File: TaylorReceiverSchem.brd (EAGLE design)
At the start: 51.7 x 73.7 mm, 16 parts, among them U1 TEENSY_3.1_BASIC, U2 XBEE_ADAPTER_KIT

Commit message: Improved PCB Routing
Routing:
- net STRIP7: track 90.1 -> 71.8 mm, vias 1 -> 0
- net 3.3V: track 41.7 -> 53.2 mm, vias 1 -> 0
- net VCC: track 41.1 -> 30.4 mm, vias 2 -> 0
- net STRIP2: track 57.8 -> 49.1 mm
- net STRIP1: track 38.5 -> 47.1 mm, vias 1 -> 0
- net GND: track 8.19 -> 0.00 mm
- net STRIP3: track 36.0 -> 43.4 mm, vias 1 -> 0
- net N$4: track 57.2 -> 52.3 mm, vias 1 -> 0
- net STRIP6: track 50.6 -> 46.6 mm, vias 0 -> 1
- net N$9: track 24.7 -> 26.2 mm
- net N$7: track 10.8 -> 12.3 mm
- net N$6: track 13.3 -> 14.8 mm
- net N$10: track 22.2 -> 23.7 mm
- net STRIP8: track 56.7 -> 55.5 mm
- net N$1: track 3.07 -> 2.54 mm

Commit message: New and improved board design
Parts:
- removed R4, R5, R6, R7, R8: (no value), SparkFun-Resistors:AXIAL-0.4
- added C3, C4: (no value), SparkFun-Capacitors:CAP-PTH-5MM
- added D1, D2, D3: (no value), SparkFun-LED:LED5MM
- added F1: (no value), fuse:SHK20L
- added RN1: (no value), resistor-dil:DIL16
- added SW1: (no value), special:EDG-04
- added U3: XBEE-1B1, SparkFun-RF:XBEE-1
- R1, R2, R3: device SparkFun-Resistors:AXIAL-0.4 -> SparkFun-Passives:AXIAL-0.3
- U2: value XBEE_ADAPTER_KIT -> V_REG_LDOSMD; device Nanotronics:1X10 -> SparkFun-PowerIC:SOT23-5
- moved C1 41.2 mm to (44.5, 68.6)
- moved U2 35.6 mm to (39.4, 68.6), turned to 180 degrees
- moved C2 18.8 mm to (24.1, 5.08), turned to 90 degrees
- moved JP1 11.4 mm to (58.4, 47.0)
- moved JP2 11.4 mm to (58.4, 20.3)
- moved JP3 11.4 mm to (58.4, 71.1)
- moved R1 6.35 mm to (30.5, 49.5), turned to 90 degrees
- moved R3 5.08 mm to (34.3, 49.5), turned to 90 degrees
- moved R2 3.81 mm to (38.1, 49.5), turned to 90 degrees
- moved JP4 1.27 mm to (33.0, 0.00)
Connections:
- removed net N$4: U1.0, U2.8
- removed net N$5: U1.1, U2.7
- new net ASC: R3.P$1, U3.15
- new net DIP1: SW1.1, U1.9
- new net DIP2: SW1.2, U1.10
- new net DIP3: SW1.3, U1.11
- new net DIP4: SW1.4, U1.12
- new net N$15: D1.A, R1.P$2
- new net N$16: D2.A, R2.P$2
- new net N$17: D3.A, R3.P$2
- new net N$2: F1.1A, JP4.PWR
- new net N$3: C3.1, C4.1, U2.5, U3.1
- new net RSSI: R2.P$1, U3.6
- new net XBEERECV: U1.0, U3.2
- net GND: now also C3.2, C4.2, D1.K, D2.K, D3.K, SW1.5, SW1.6, SW1.7, SW1.8, U3.10, U3.3; no longer U2.4
- net N$10: now also RN1.5; no longer R5.P$1
- net N$11: now also RN1.6; no longer R6.P$1
- net N$12: now also RN1.7; no longer R7.P$1
- net N$13: now also RN1.8; no longer R8.P$1
- net N$6: now also RN1.1; no longer R1.P$1
- net N$7: now also RN1.2; no longer R2.P$1
- net N$8: now also RN1.3; no longer R3.P$1
- net N$9: now also RN1.4; no longer R4.P$1
- net STRIP1: now also RN1.16; no longer R1.P$2
- net STRIP2: now also RN1.15; no longer R2.P$2
- net STRIP3: now also RN1.14; no longer R3.P$2
- net STRIP4: now also RN1.13; no longer R4.P$2
- net STRIP5: now also RN1.12; no longer R5.P$2
- net STRIP6: now also RN1.11; no longer R6.P$2
- net STRIP7: now also RN1.10; no longer R7.P$2
- net STRIP8: now also RN1.9; no longer R8.P$2
- net VCC: now also F1.2A, R1.P$1, U2.3; no longer JP4.PWR, U2.10
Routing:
- net XBEERECV: track 0.00 -> 75.6 mm
- net N$4: track 52.3 -> 0.00 mm
- net N$5: track 52.3 -> 0.00 mm
- net DIP1: track 0.00 -> 50.9 mm, vias 0 -> 1
- net RSSI: track 0.00 -> 43.3 mm
- net N$3: track 0.00 -> 41.0 mm
- net DIP2: track 0.00 -> 36.7 mm
- net DIP3: track 0.00 -> 33.1 mm, vias 0 -> 1
- net VCC: track 30.4 -> 0.00 mm
- net DIP4: track 0.00 -> 28.0 mm
- net N$13: track 8.15 -> 35.4 mm
- net N$12: track 8.15 -> 30.0 mm
- net N$8: track 10.8 -> 31.6 mm
- net STRIP1: track 47.1 -> 27.3 mm
- net STRIP3: track 43.4 -> 24.1 mm
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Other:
- board size 51.7 x 73.7 mm -> 61.9 x 73.7 mm
- board text added: "ASC"
- board text added: "Asher Levine"
- board text added: "David Sheinkopf"
- board text added: "GND"
- board text added: "Power"
- board text added: "RSSI"
- board text added: "VCC"
- board text added: "XBEE"
- board text removed: "Dave Sheinkopf"

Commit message: Added right angle connectors to board.
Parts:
- removed JP1, JP2, JP3: (no value), SparkFun-Connectors:1X08_ROUND
- added P1, P2, P3: 39-30-08?_S, con-molex-mini-fit:39-30-?08?
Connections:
- removed net N$10: JP2.3, RN1.5
- removed net N$11: JP2.1, RN1.6
- new net N$4: P2.5, RN1.5
- new net N$5: P2.2, RN1.6
- net GND: now also P1.3, P1.7, P2.3, P2.7, P3.3, P3.7; no longer JP1.4, JP1.7, JP2.4, JP2.7, JP3.4, JP3.7
- net N$12: now also P3.6; no longer JP3.6
- net N$13: now also P3.5; no longer JP3.3
- net N$6: now also P1.6; no longer JP1.6
- net N$7: now also P1.5; no longer JP1.3
- net N$8: now also P1.2; no longer JP1.1
- net N$9: now also P2.6; no longer JP2.6
- net VCC: now also P1.1, P1.4, P1.8, P2.1, P2.4, P2.8, P3.4, P3.8; no longer JP1.2, JP1.5, JP1.8, JP2.2, JP2.5, JP2.8, JP3.5, JP3.8
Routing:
- net N$6: track 21.2 -> 108.4 mm
- net N$7: track 25.5 -> 89.5 mm
- net N$5: track 0.00 -> 37.5 mm
- net VCC: track 0.00 -> 25.1 mm, vias 0 -> 1
- net N$4: track 0.00 -> 19.4 mm
- net N$10: track 16.6 -> 0.00 mm
- net N$13: track 35.4 -> 19.6 mm
- net N$8: track 31.6 -> 47.1 mm
- net N$11: track 14.8 -> 0.00 mm
- net N$12: track 30.0 -> 21.2 mm
- net N$9: track 22.4 -> 17.0 mm
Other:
- board size 61.9 x 73.7 mm -> 70.8 x 73.7 mm

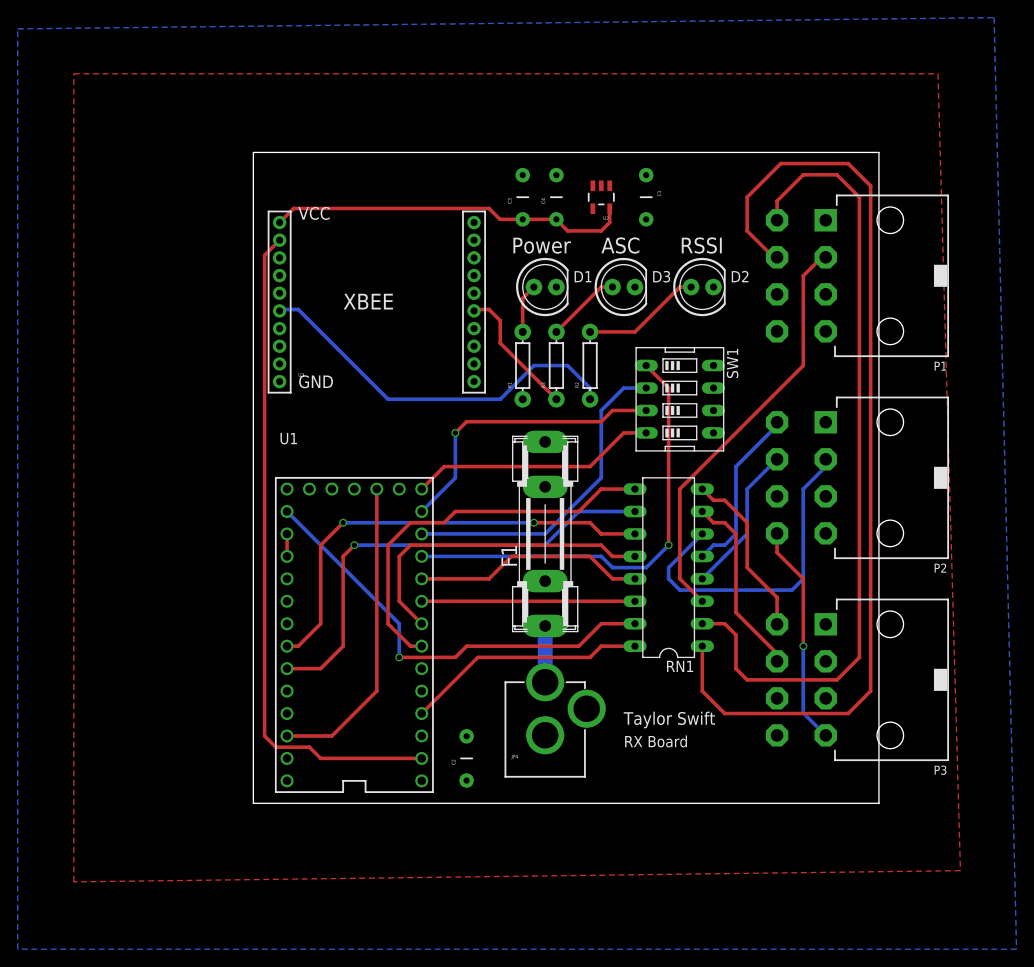
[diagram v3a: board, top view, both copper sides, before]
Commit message: Added mounting holes.
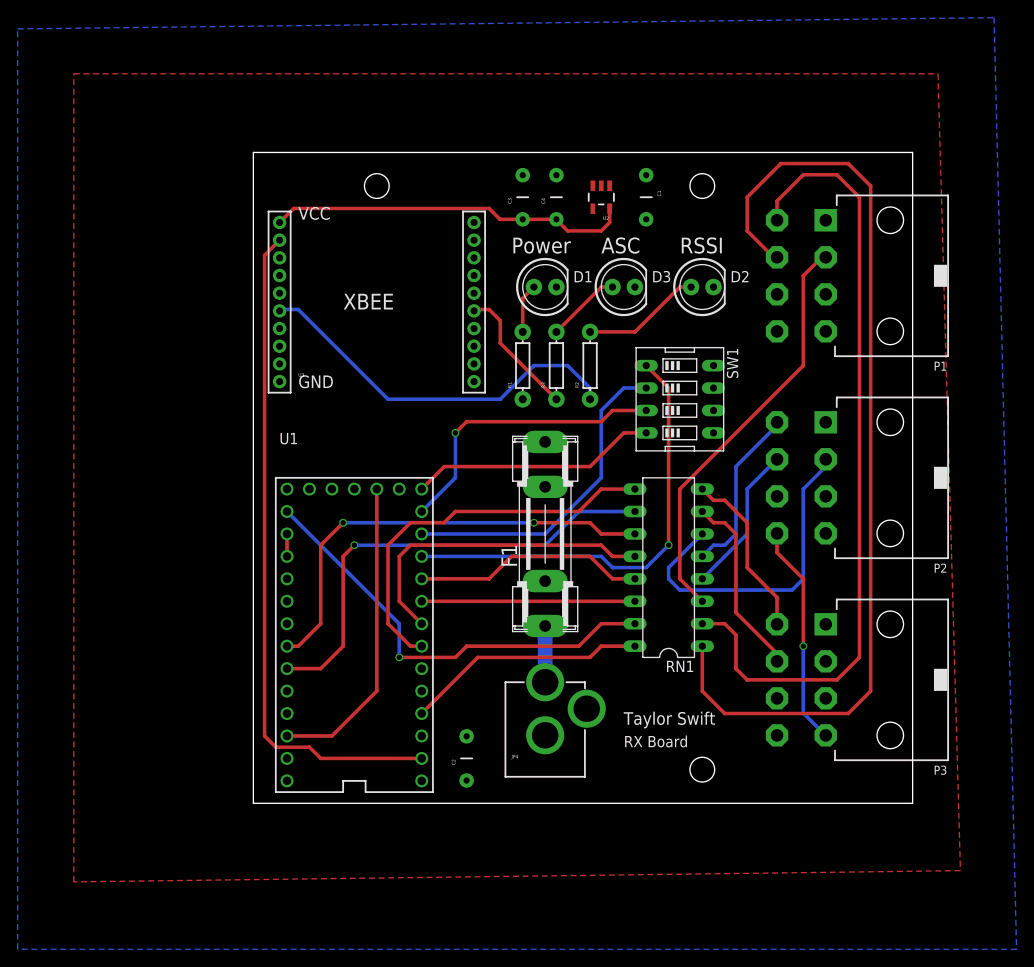
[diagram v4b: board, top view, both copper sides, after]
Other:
- board size 70.8 x 73.7 mm -> 74.6 x 73.7 mm
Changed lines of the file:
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@@
 <setting verticaltext="up"/>
 </settings>
-<grid distance="0.05" unitdist="inch" unit="inch" style="lines" multiple="1" display="no" altdistance="0.025" altunitdist="inch" altunit="inch"/>
+<grid distance="0.05" unitdist="inch" unit="mm" style="lines" multiple="1" display="no" altdistance="0.025" altunitdist="inch" altunit="mm"/>
 <layers>
 <layer number="1" name="Top" color="4" fill="1" visible="yes" active="yes"/>
@@
 <layer number="43" name="vRestrict" color="2" fill="10" visible="yes" active="yes"/>
 <layer number="44" name="Drills" color="7" fill="1" visible="no" active="yes"/>
-<layer number="45" name="Holes" color="7" fill="1" visible="no" active="yes"/>
+<layer number="45" name="Holes" color="7" fill="1" visible="yes" active="yes"/>
 <layer number="46" name="Milling" color="3" fill="1" visible="no" active="yes"/>
 <layer number="47" name="Measures" color="7" fill="1" visible="no" active="yes"/>
@@
 <board>
 <plain>
-<wire x1="0" y1="0" x2="70.79" y2="0" width="0" layer="20"/>
-<wire x1="70.79" y1="0" x2="70.79" y2="73.65" width="0" layer="20"/>
-<wire x1="70.79" y1="73.65" x2="0" y2="73.65" width="0" layer="20"/>
+<wire x1="0" y1="0" x2="74.6" y2="0" width="0" layer="20"/>
+<wire x1="74.6" y1="0" x2="74.6" y2="73.65" width="0" layer="20"/>
+<wire x1="74.6" y1="73.65" x2="0" y2="73.65" width="0" layer="20"/>
 <wire x1="0" y1="73.65" x2="0" y2="0" width="0" layer="20"/>
 <text x="29.21" y="62.23" size="1.778" layer="21">Power</text>
@@
 <text x="11.43" y="46.99" size="1.4224" layer="22" rot="MR90">David Sheinkopf</text>
 <text x="19.05" y="46.99" size="1.4224" layer="22" rot="MR90">Dylan Fashbaugh</text>
+<hole x="50.8" y="69.85" drill="2.8"/>
+<hole x="13.97" y="69.85" drill="2.8"/>
+<hole x="50.8" y="3.81" drill="2.8"/>
 </plain>
 <attributes>

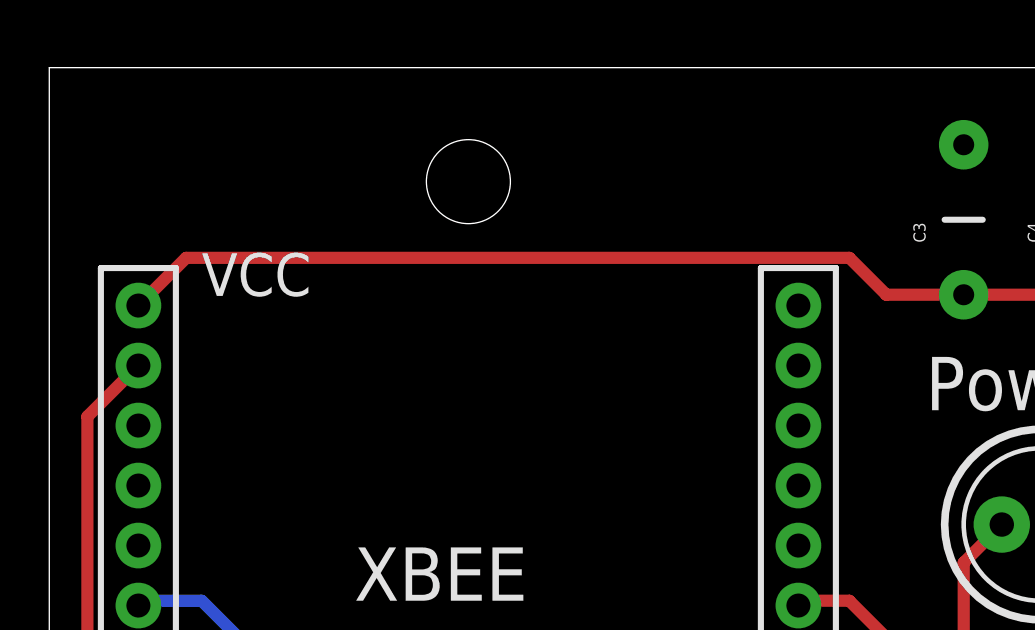
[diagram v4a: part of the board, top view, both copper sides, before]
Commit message: Moved the traces a safe distance from mounting holes.
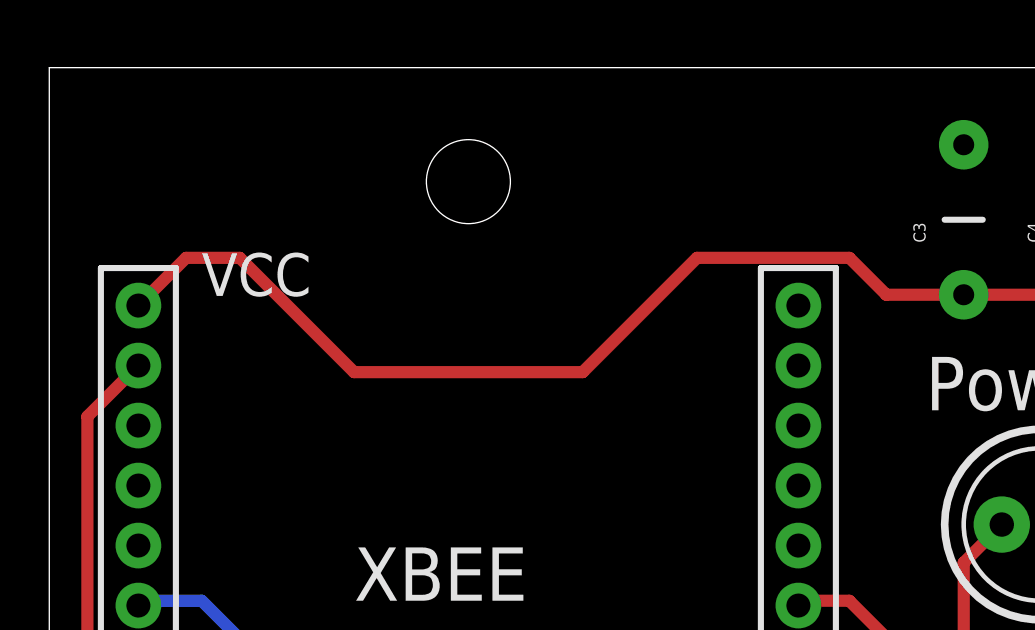
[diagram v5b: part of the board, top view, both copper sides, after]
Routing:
- net N$3: track 41.0 -> 44.2 mm
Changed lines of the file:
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@@
 <wire x1="30.48" y1="66.08" x2="27.9" y2="66.08" width="0.4064" layer="1"/>
 <wire x1="27.9" y1="66.08" x2="26.67" y2="67.31" width="0.4064" layer="1"/>
-<wire x1="26.67" y1="67.31" x2="4.56" y2="67.31" width="0.4064" layer="1"/>
 <wire x1="4.56" y1="67.31" x2="2.97" y2="65.72" width="0.4064" layer="1"/>
 <wire x1="40.32" y1="67.2799" x2="40.32" y2="65.72" width="0.4064" layer="1"/>
@@
 <wire x1="35.56" y1="64.77" x2="34.29" y2="66.04" width="0.4064" layer="1"/>
 <wire x1="34.29" y1="66.04" x2="34.29" y2="66.08" width="0.4064" layer="1"/>
+<wire x1="4.56" y1="67.31" x2="6.35" y2="67.31" width="0.4064" layer="1"/>
+<wire x1="6.35" y1="67.31" x2="10.16" y2="63.5" width="0.4064" layer="1"/>
+<wire x1="10.16" y1="63.5" x2="17.78" y2="63.5" width="0.4064" layer="1"/>
+<wire x1="17.78" y1="63.5" x2="21.59" y2="67.31" width="0.4064" layer="1"/>
+<wire x1="21.59" y1="67.31" x2="26.67" y2="67.31" width="0.4064" layer="1"/>
 </signal>
 <signal name="ASC">
